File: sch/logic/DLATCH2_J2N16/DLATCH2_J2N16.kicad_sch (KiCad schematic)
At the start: 9 parts

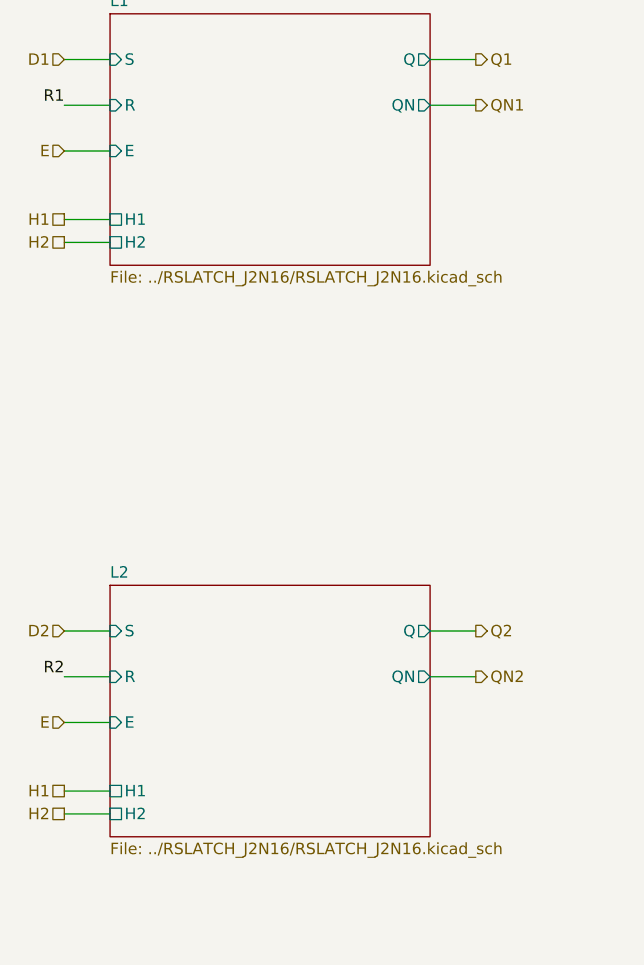
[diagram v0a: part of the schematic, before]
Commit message: DFFRN_J2N16X7 / DFFSN_J2N16X7: async clear / preset through a 6Kh7B (REQ-MOD-004/005/008)
- DFF_J2N16 + one 6Kh7B: a diode from the reset line into FQN (clear) or
  FQ (preset) of both latches; Cc 2.7 pF across each feedback divider
  compensates the diode capacitance (without it 1 MHz fails)
- reset line: idle -20 V (owner), GND = asserted; RN/SN active low, so
  rst_n drives them with no inverter
- tools/spice/dffr_sweep.py: normal / async / recovery; RN -> Q 54-100 ns,
  SN -> Q 273-611 ns, recovery >= 100 ns before C falls
- RSLATCH sheet brings FQ/FQN out; KiCad sheets and benches agree with
  plain SPICE; 6Kh7B symbol and the two-diode model 6Kh7B2
- liberty replaces DFFSR/DFFSR_n; vtube_level RESET (div_insert: no
  divider, port-driven check); SDF and checker modes 3/4
- run_tests.sh -s: 1400.5 tubes + 5 relays (+38 diodes), equiv proven

Co-Authored-By: Claude Opus 5.5 <noreply@anthropic.com>
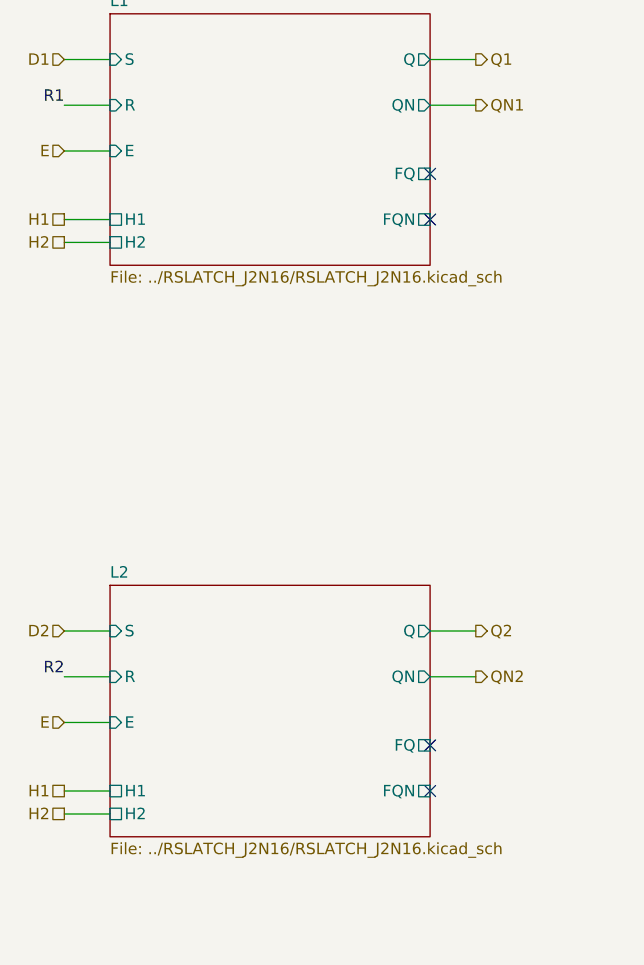
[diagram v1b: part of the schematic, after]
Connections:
- no-connect marks 0 -> 4
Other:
- sheet L1 ports: added FQ, FQN; removed none
- sheet L2 ports: added FQ, FQN; removed none
